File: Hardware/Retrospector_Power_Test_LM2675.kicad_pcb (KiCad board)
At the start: 2 copper layers, 27 x 25 mm, 21 parts, among them J2 Eurorack_10_pin_power, U1 TPS5410D, U2 LD1117-3.3-4Tab

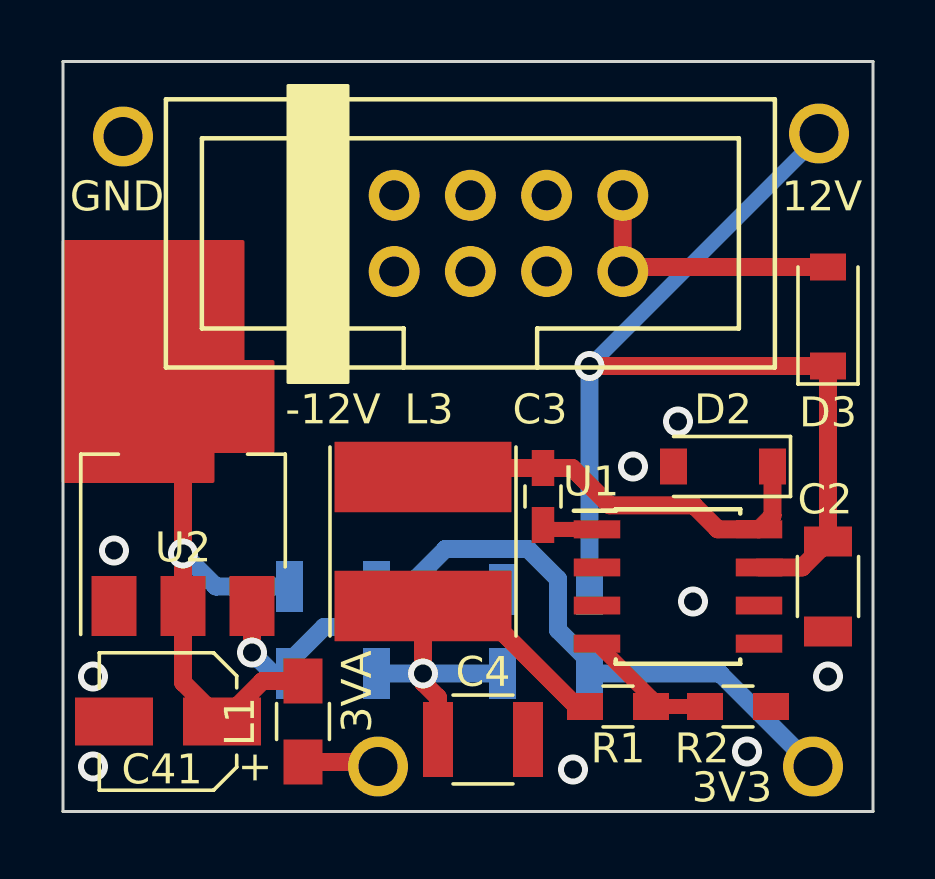
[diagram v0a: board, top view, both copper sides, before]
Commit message: Power test PCBs finished and sent to production; basic implementation of clocked delay
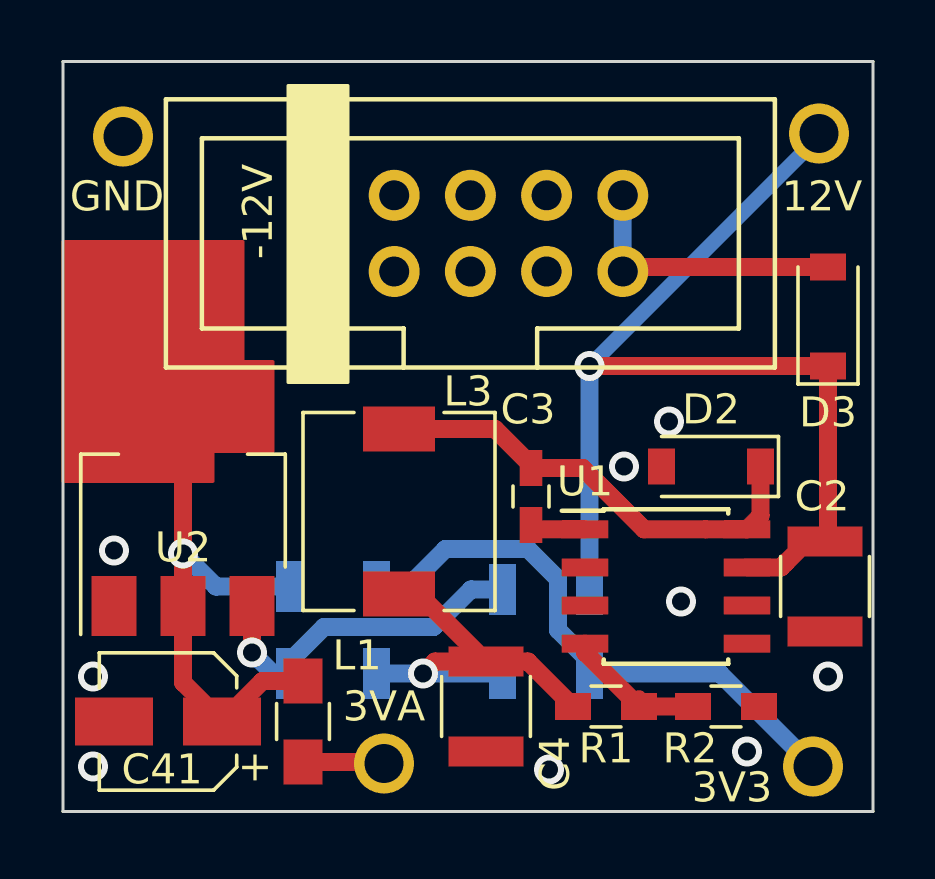
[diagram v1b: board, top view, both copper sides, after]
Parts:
- C2: footprint Capacitors_SMD:C_1206 -> Capacitors_SMD:C_1210
- L3: value 56uH -> 47uH; footprint Custom_Footprints:Inductor_SMD_6x6mm -> Inductors_SMD:L_6.3x6.3_H3
- R1: value 10k -> 1.74k
- R2: value 5.9k -> 1k
- U1: value TPS5410D -> LM2675M-ADJ
- moved L3 1.28 mm to (96.2, 64.0)
- moved C4 1.10 mm to (99.1, 70.5), turned to 270 degrees
- moved C3 0.40 mm to (100.6, 63.5)
- moved D2 0.40 mm to (106.6, 62.5)
- moved R1 0.40 mm to (103.1, 70.5)
- moved R2 0.40 mm to (107.1, 70.5)
- moved U1 0.40 mm to (105.1, 66.5)
- moved TP3 0.22 mm to (95.7, 72.4)
- moved C2 0.10 mm to (110.4, 66.5)
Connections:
- net /BOOT renamed /CB
- net /PH renamed /VSW
- net /VSENSE renamed /FB
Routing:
- net /V_Int: track 16.6 -> 14.0 mm
- net /VSW: track 14.5 -> 15.4 mm
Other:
- board text added: "Power Test v1 TPS5410D / LM2675"
- board text removed: "Power Test v1 TPS5410D"
